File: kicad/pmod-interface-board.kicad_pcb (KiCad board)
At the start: 4 copper layers, 81.7 x 61 mm, 30 parts, among them J1 PMOD Connector 1, J2 PMOD Connector 2, J4 Gameboy Cart Connector, U1 74HCT541, U2 74HCT541, U3 74HC595, U4 74HC595, U5 74HC595, U6 74HC597

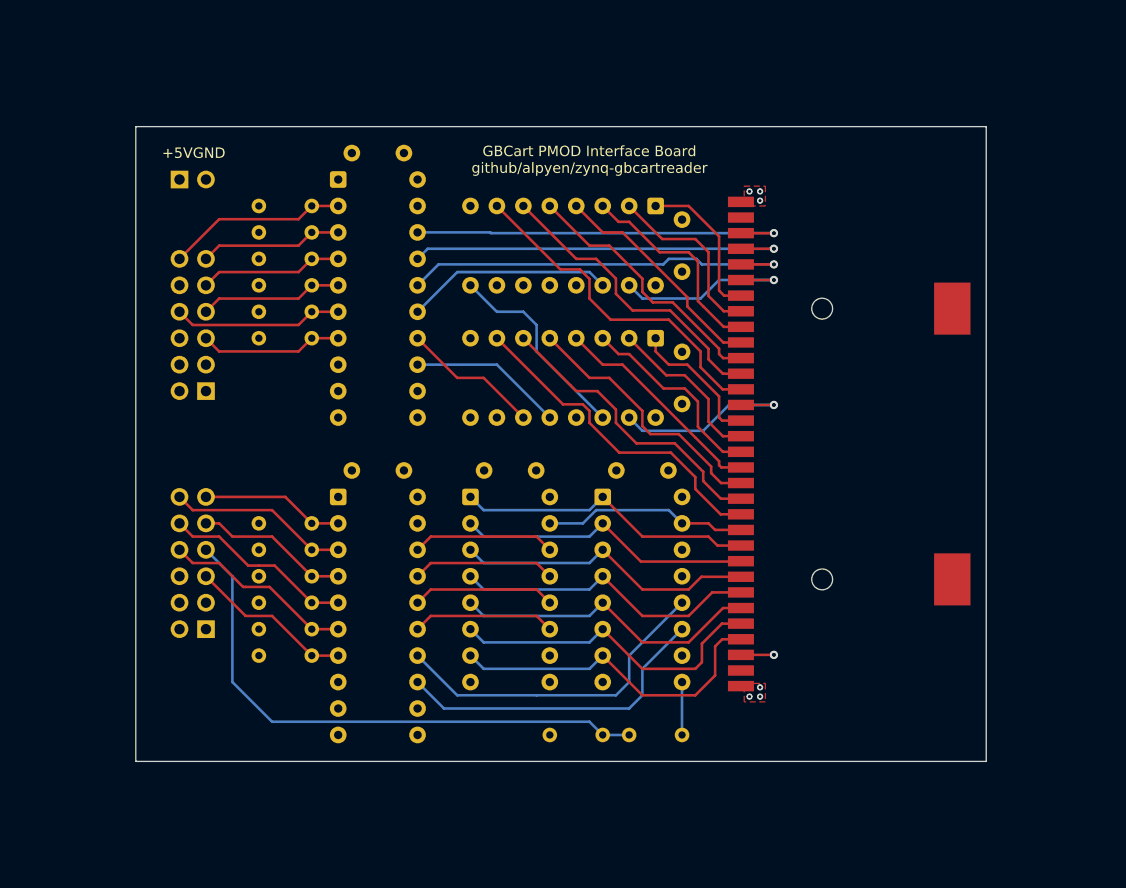
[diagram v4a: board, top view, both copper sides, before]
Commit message: kicad: moved resistor divider and added gnd stitching vias
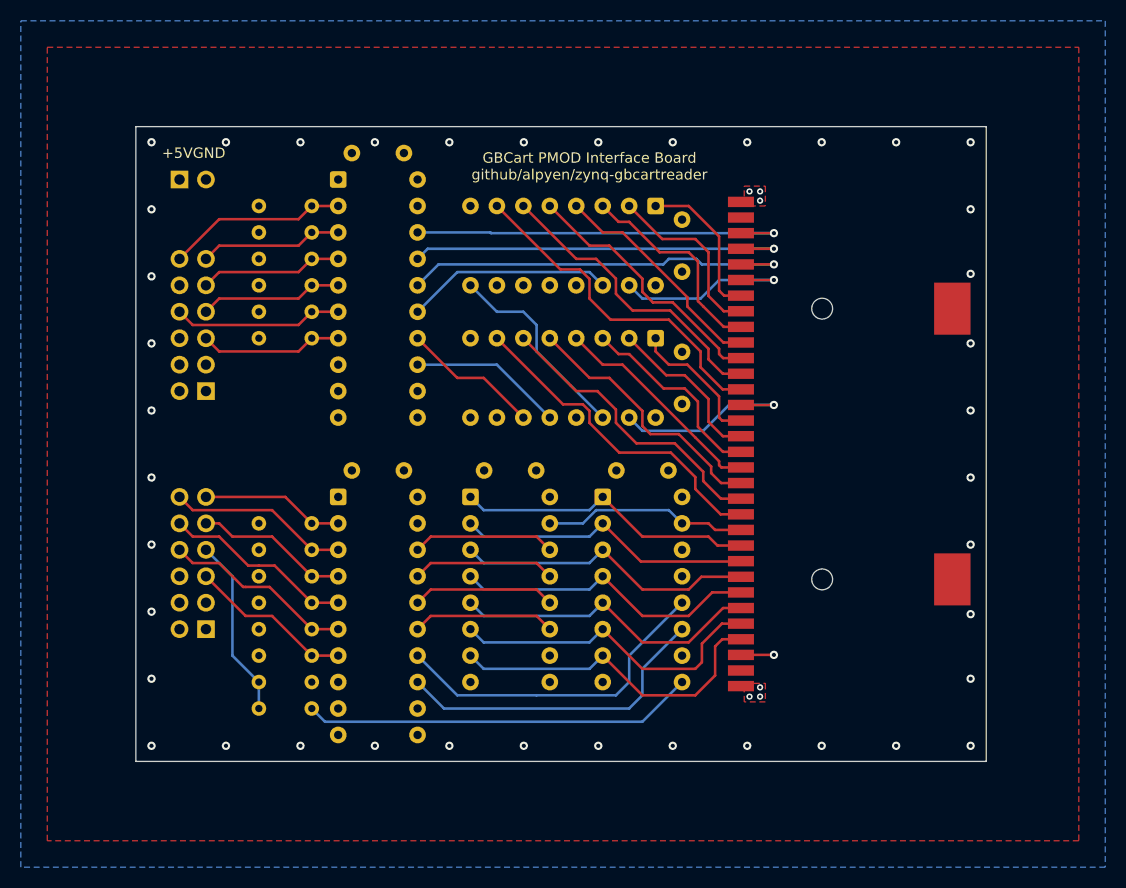
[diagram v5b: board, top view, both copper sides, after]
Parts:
- moved R13 35.7 mm to (127.0, 116.8)
- moved R14 33.4 mm to (121.9, 114.3), turned to 0 degrees
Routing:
- net DATA_IN_SDATA_out: track 54.0 -> 17.3 mm
- net Net-(U6-Q7): track 5.08 -> 37.7 mm
- net GND: vias 3 -> 43
- added copper zone on B.Cu, net GND
